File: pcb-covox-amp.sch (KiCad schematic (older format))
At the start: 41 parts, among them J1 DB25, P1 USB_OTG, U1 LM386, X1 MJ-2135MJ-2135, X2 MJ-2135MJ-2135

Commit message: another commit
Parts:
- D1: value Yellow LED -> Yellow
- P1: value USB_OTG -> USB
- X1: value MJ-2135MJ-2135 -> Amp
- X2: value MJ-2135MJ-2135 -> Raw
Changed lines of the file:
@@
 P 10700 1300
 F 0 "X2" H 10500 900 45  0000 L BNN
-F 1 "MJ-2135MJ-2135" H 10700 1300 45  0001 L BNN
+F 1 "Raw" H 10700 1300 45  0001 L BNN
 F 2 "mj2135:mj-2135-MJ-2135" H 10730 1450 20  0001 C CNN
 F 3 "" H 10700 1300 60  0000 C CNN
@@
 P 7400 1650
 F 0 "P1" H 7725 1525 50  0000 C CNN
-F 1 "USB_OTG" H 7400 1850 50  0000 C CNN
+F 1 "USB" H 7400 1850 50  0000 C CNN
 F 2 "Connect:USB_Micro-B" V 7350 1550 50  0001 C CNN
 F 3 "" V 7350 1550 50  0000 C CNN
@@
 P 10650 2750
 F 0 "X1" H 10450 2350 45  0000 L BNN
-F 1 "MJ-2135MJ-2135" H 10650 2750 45  0001 L BNN
+F 1 "Amp" H 10650 2750 45  0001 L BNN
 F 2 "mj2135:mj-2135-MJ-2135" H 10680 2900 20  0001 C CNN
 F 3 "" H 10650 2750 60  0000 C CNN
@@
 P 7800 2450
 F 0 "D1" H 7800 2550 50  0000 C CNN
-F 1 "Yellow LED" H 7800 2350 50  0000 C CNN
+F 1 "Yellow" H 7800 2350 50  0000 C CNN
 F 2 "LEDs:LED_0805" H 7800 2450 50  0001 C CNN
 F 3 "" H 7800 2450 50  0000 C CNN

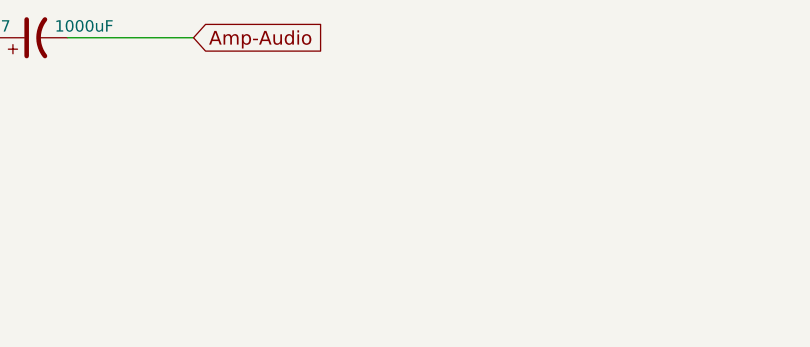
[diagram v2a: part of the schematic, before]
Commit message: add mounting holes rev 2
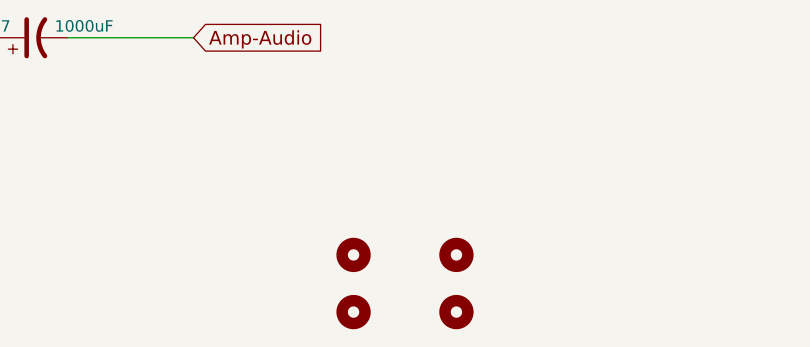
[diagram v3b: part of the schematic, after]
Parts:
- added MH1, MH2, MH3, MH4: MOUNTHOLE, Mounting_Holes:MountingHole_3.2mm_M3_ISO14580_Pad, symbol MOUNTHOLE
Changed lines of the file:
@@
 LIBS:valves
 LIBS:mj-2135
+LIBS:mounthole
 LIBS:pcb-covox-amp-cache
 EELAYER 25 0
@@
 Sheet 1 1
 Title "Covox with Amplifier"
-Date "2016-07-02"
-Rev "1"
+Date "2016-07-03"
+Rev "2"
 Comp ""
 Comment1 "Designed by Yeo Kheng Meng"
@@
 Wire Wire Line
 	7300 950  7400 950
+$Comp
+L MOUNTHOLE MH1
+U 1 1 5778DB2B
+P 5650 7000
+F 0 "MH1" H 5800 7050 50  0001 C CNN
+F 1 "MOUNTHOLE" H 5650 7150 50  0001 C CNN
+F 2 "Mounting_Holes:MountingHole_3.2mm_M3_ISO14580_Pad" H 5650 7000 50  0001 C CNN
+F 3 "" H 5650 7000 50  0000 C CNN
+	1    5650 7000
+	1    0    0    -1
+$EndComp
+$Comp
+L MOUNTHOLE MH3
+U 1 1 5778DB91
+P 6100 7000
+F 0 "MH3" H 6250 7050 50  0001 C CNN
+F 1 "MOUNTHOLE" H 6100 7150 50  0001 C CNN
+F 2 "Mounting_Holes:MountingHole_3.2mm_M3_ISO14580_Pad" H 6100 7000 50  0001 C CNN
+F 3 "" H 6100 7000 50  0000 C CNN
+	1    6100 7000
+	1    0    0    -1
+$EndComp
+$Comp
+L MOUNTHOLE MH2
+U 1 1 5778DBF7
+P 5650 7250
+F 0 "MH2" H 5800 7300 50  0001 C CNN
+F 1 "MOUNTHOLE" H 5650 7400 50  0001 C CNN
+F 2 "Mounting_Holes:MountingHole_3.2mm_M3_ISO14580_Pad" H 5650 7250 50  0001 C CNN
+F 3 "" H 5650 7250 50  0000 C CNN
+	1    5650 7250
+	1    0    0    -1
+$EndComp
+$Comp
+L MOUNTHOLE MH4
+U 1 1 5778DC5D
+P 6100 7250
+F 0 "MH4" H 6250 7300 50  0001 C CNN
+F 1 "MOUNTHOLE" H 6100 7400 50  0001 C CNN
+F 2 "Mounting_Holes:MountingHole_3.2mm_M3_ISO14580_Pad" H 6100 7250 50  0001 C CNN
+F 3 "" H 6100 7250 50  0000 C CNN
+	1    6100 7250
+	1    0    0    -1
+$EndComp
 $EndSCHEMATC

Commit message: update db25 package
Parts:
- J1: footprint Connect:DB25MC -> db25:DB25MC
- RV1, RV2, RV3: symbol POT -> POT-RESCUE-pcb-covox-amp
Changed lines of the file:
@@
 Sheet 1 1
 Title "Covox with Amplifier"
-Date "2016-07-03"
+Date "2016-07-11"
 Rev "2"
 Comp ""
@@
 F 0 "J1" H 1050 3300 50  0000 C CNN
 F 1 "DB25" H 950 600 50  0000 C CNN
-F 2 "Connect:DB25MC" H 1000 1950 50  0001 C CNN
+F 2 "db25:DB25MC" H 1000 1950 50  0001 C CNN
 F 3 "" H 1000 1950 50  0000 C CNN
 	1    1000 1950
@@
 $EndComp
 $Comp
-L POT RV1
+L POT-RESCUE-pcb-covox-amp RV1
 U 1 1 5777A309
 P 6850 5000
@@
 $EndComp
 $Comp
-L POT RV2
+L POT-RESCUE-pcb-covox-amp RV2
 U 1 1 5777A420
 P 9050 5000
@@
 Input+
 $Comp
-L POT RV3
+L POT-RESCUE-pcb-covox-amp RV3
 U 1 1 5778C8B1
 P 10450 5000

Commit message: adjust foot print
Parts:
- C10, C5: footprint Capacitors_SMD:c_elec_10x10.5 -> Capacitors_SMD:c_elec_4x5.3
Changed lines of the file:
@@
 F 0 "C5" V 3700 5400 50  0000 L CNN
 F 1 "10uF" V 3700 5100 50  0000 L CNN
-F 2 "Capacitors_SMD:c_elec_10x10.5" H 3650 5350 50  0001 C CNN
+F 2 "Capacitors_SMD:c_elec_4x5.3" H 3650 5350 50  0001 C CNN
 F 3 "" H 3650 5350 50  0000 C CNN
 	1    3650 5350
@@
 F 0 "C10" V 8550 5050 50  0000 L CNN
 F 1 "10uF" V 8550 4750 50  0000 L CNN
-F 2 "Capacitors_SMD:c_elec_10x10.5" H 8500 5000 50  0001 C CNN
+F 2 "Capacitors_SMD:c_elec_4x5.3" H 8500 5000 50  0001 C CNN
 F 3 "" H 8500 5000 50  0000 C CNN
 	1    8500 5000

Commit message: adjust add pot direction
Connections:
- net GND: now also RV1.1; no longer RV1.3
- net Gain1: now also RV3.3; no longer RV3.1
- net Source-Audio: now also RV1.3; no longer RV1.1
- net at RV2.1: no longer C10.1
- net at RV2.3: now also C10.1
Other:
- moved on the sheet: C10, C11, RV1, RV2, RV3
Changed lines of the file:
@@
 L POT-RESCUE-pcb-covox-amp RV1
 U 1 1 5777A309
-P 6850 5000
-F 0 "RV1" H 6850 4900 50  0000 C CNN
-F 1 "10K" H 6850 5000 50  0000 C CNN
-F 2 "Potentiometers:Potentiometer_Alps-RK163-single_15mm" H 6850 5000 50  0001 C CNN
-F 3 "" H 6850 5000 50  0000 C CNN
-F 4 "Volume" H 6850 4800 60  0000 C CNN "Purpose"
-	1    6850 5000
+P 6150 4950
+F 0 "RV1" H 6150 4850 50  0000 C CNN
+F 1 "10K" H 6150 4950 50  0000 C CNN
+F 2 "Potentiometers:Potentiometer_Alps-RK163-single_15mm" H 6150 4950 50  0001 C CNN
+F 3 "" H 6150 4950 50  0000 C CNN
+F 4 "Volume" H 6150 4750 60  0000 C CNN "Purpose"
+	1    6150 4950
 	1    0    0    -1
 $EndComp
@@
 L POT-RESCUE-pcb-covox-amp RV2
 U 1 1 5777A420
-P 9050 5000
-F 0 "RV2" H 9050 4900 50  0000 C CNN
-F 1 "10K" H 9050 5000 50  0000 C CNN
-F 2 "Potentiometers:Potentiometer_Alps-RK163-single_15mm" H 9050 5000 50  0001 C CNN
-F 3 "" H 9050 5000 50  0000 C CNN
-F 4 "Gain" H 9050 4800 60  0000 C CNN "Purpose"
-	1    9050 5000
+P 7850 4950
+F 0 "RV2" H 7850 4850 50  0000 C CNN
+F 1 "10K" H 7850 4950 50  0000 C CNN
+F 2 "Potentiometers:Potentiometer_Alps-RK163-single_15mm" H 7850 4950 50  0001 C CNN
+F 3 "" H 7850 4950 50  0000 C CNN
+F 4 "Gain" H 7850 4750 60  0000 C CNN "Purpose"
+	1    7850 4950
 	1    0    0    -1
 $EndComp
@@
 L GND #PWR08
 U 1 1 57781DE3
-P 7200 5150
-F 0 "#PWR08" H 7200 4900 50  0001 C CNN
-F 1 "GND" H 7200 5000 50  0000 C CNN
-F 2 "" H 7200 5150 50  0000 C CNN
-F 3 "" H 7200 5150 50  0000 C CNN
-	1    7200 5150
-	1    0    0    -1
-$EndComp
-Text GLabel 6250 5000 0    60   Input ~ 0
+P 5750 5000
+F 0 "#PWR08" H 5750 4750 50  0001 C CNN
+F 1 "GND" H 5750 4850 50  0000 C CNN
+F 2 "" H 5750 5000 50  0000 C CNN
+F 3 "" H 5750 5000 50  0000 C CNN
+	1    5750 5000
+	1    0    0    -1
+$EndComp
+Text GLabel 6500 4950 2    60   Input ~ 0
 Source-Audio
-Text GLabel 6850 4700 1    60   Input ~ 0
+Text GLabel 6150 4650 1    60   Input ~ 0
 Input+
 Text GLabel 1450 5900 0    60   Input ~ 0
@@
 L POT-RESCUE-pcb-covox-amp RV3
 U 1 1 5778C8B1
-P 10450 5000
-F 0 "RV3" H 10450 4900 50  0000 C CNN
-F 1 "10K" H 10450 5000 50  0000 C CNN
-F 2 "Potentiometers:Potentiometer_Alps-RK163-single_15mm" H 10450 5000 50  0001 C CNN
-F 3 "" H 10450 5000 50  0000 C CNN
-F 4 "Bass" H 10450 4800 60  0000 C CNN "Purpose"
-	1    10450 5000
+P 9900 4950
+F 0 "RV3" H 9900 4850 50  0000 C CNN
+F 1 "10K" H 9900 4950 50  0000 C CNN
+F 2 "Potentiometers:Potentiometer_Alps-RK163-single_15mm" H 9900 4950 50  0001 C CNN
+F 3 "" H 9900 4950 50  0000 C CNN
+F 4 "Bass" H 9900 4750 60  0000 C CNN "Purpose"
+	1    9900 4950
 	1    0    0    -1
 $EndComp
@@
 	2750 6300 2750 6850
 Wire Wire Line
-	7100 5000 7200 5000
-Wire Wire Line
-	7200 5000 7200 5150
-Wire Wire Line
-	6600 5000 6250 5000
-Wire Wire Line
-	6850 4850 6850 4700
+	6150 4800 6150 4650
 Wire Wire Line
 	1450 5900 2450 5900
@@
 	2950 6350 2950 6300
 Wire Wire Line
-	9050 4850 9050 4600
+	7850 4800 7850 4550
 $Comp
 L CP1 C10
 U 1 1 577AE6CB
-P 8500 5000
-F 0 "C10" V 8550 5050 50  0000 L CNN
-F 1 "10uF" V 8550 4750 50  0000 L CNN
-F 2 "Capacitors_SMD:c_elec_4x5.3" H 8500 5000 50  0001 C CNN
-F 3 "" H 8500 5000 50  0000 C CNN
-	1    8500 5000
-	0    1    1    0
-$EndComp
-Wire Wire Line
-	8800 5000 8650 5000
-Text GLabel 9050 4600 1    60   Input ~ 0
+P 8500 4950
+F 0 "C10" V 8550 5000 50  0000 L CNN
+F 1 "10uF" V 8550 4700 50  0000 L CNN
+F 2 "Capacitors_SMD:c_elec_4x5.3" H 8500 4950 50  0001 C CNN
+F 3 "" H 8500 4950 50  0000 C CNN
+	1    8500 4950
+	0    -1   -1   0
+$EndComp
+Wire Wire Line
+	8100 4950 8350 4950
+Text GLabel 7850 4550 1    60   Input ~ 0
 Gain1
-Text GLabel 8200 5000 0    60   Input ~ 0
+Text GLabel 8800 4950 2    60   Input ~ 0
 Gain8
 Wire Wire Line
-	8350 5000 8200 5000
+	8650 4950 8800 4950
 $Comp
 L C C11
 U 1 1 577B1E46
-P 10450 4450
-F 0 "C11" H 10475 4550 50  0000 L CNN
-F 1 "33000pF" H 10475 4350 50  0000 L CNN
-F 2 "Capacitors_SMD:C_0805_HandSoldering" H 10488 4300 50  0001 C CNN
-F 3 "" H 10450 4450 50  0000 C CNN
-	1    10450 4450
-	1    0    0    -1
-$EndComp
-Wire Wire Line
-	10450 4850 10450 4600
-Text GLabel 10450 4100 1    60   Input ~ 0
+P 9900 4400
+F 0 "C11" H 9925 4500 50  0000 L CNN
+F 1 "33000pF" H 9925 4300 50  0000 L CNN
+F 2 "Capacitors_SMD:C_0805_HandSoldering" H 9938 4250 50  0001 C CNN
+F 3 "" H 9900 4400 50  0000 C CNN
+	1    9900 4400
+	1    0    0    -1
+$EndComp
+Wire Wire Line
+	9900 4800 9900 4550
+Text GLabel 9900 4050 1    60   Input ~ 0
 Vout
 Wire Wire Line
-	10450 4300 10450 4100
-Text GLabel 10100 5000 0    60   Input ~ 0
+	9900 4250 9900 4050
+Text GLabel 10250 4950 2    60   Input ~ 0
 Gain1
-Wire Wire Line
-	10200 5000 10100 5000
 Text GLabel 9500 2650 0    60   Input ~ 0
 Amp-Audio
@@
 	1    0    0    -1
 $EndComp
+Wire Wire Line
+	6400 4950 6500 4950
+Wire Wire Line
+	5900 4950 5750 4950
+Wire Wire Line
+	5750 4950 5750 5000
+Wire Wire Line
+	10250 4950 10150 4950
 $EndSCHEMATC

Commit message: assign all parallel pout ground pins and rev 3
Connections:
- net GND: now also J1.18 (P18), J1.20 (P20), J1.21 (P21), J1.22 (P22), J1.23 (P23), J1.24 (P24), J1.25 (P25)
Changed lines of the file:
@@
 Sheet 1 1
 Title "Covox with Amplifier"
-Date "2016-07-11"
-Rev "2"
+Date "2016-07-24"
+Rev "3"
 Comp ""
 Comment1 "Designed by Yeo Kheng Meng"
@@
 L GND #PWR01
 U 1 1 57761E43
-P 2100 2100
-F 0 "#PWR01" H 2100 1850 50  0001 C CNN
-F 1 "GND" H 2100 1950 50  0000 C CNN
-F 2 "" H 2100 2100 50  0000 C CNN
-F 3 "" H 2100 2100 50  0000 C CNN
-	1    2100 2100
+P 2100 3300
+F 0 "#PWR01" H 2100 3050 50  0001 C CNN
+F 1 "GND" H 2100 3150 50  0000 C CNN
+F 2 "" H 2100 3300 50  0000 C CNN
+F 3 "" H 2100 3300 50  0000 C CNN
+	1    2100 3300
 	1    0    0    -1
 $EndComp
@@
 	1450 1850 2100 1850
 Wire Wire Line
-	2100 1850 2100 2100
+	2100 1650 2100 3300
 Wire Wire Line
 	1450 2350 1600 2350
@@
 Wire Wire Line
 	10250 4950 10150 4950
+Wire Wire Line
+	1450 1650 2100 1650
+Connection ~ 2100 1850
+Wire Wire Line
+	1450 2050 2100 2050
+Connection ~ 2100 2050
+Wire Wire Line
+	1450 2450 2100 2450
+Connection ~ 2100 2450
+Wire Wire Line
+	1450 2250 2100 2250
+Connection ~ 2100 2250
+Wire Wire Line
+	1450 2650 2100 2650
+Connection ~ 2100 2650
+Wire Wire Line
+	1450 2850 2100 2850
+Connection ~ 2100 2850
+Wire Wire Line
+	1450 3050 2100 3050
+Connection ~ 2100 3050
 $EndSCHEMATC
